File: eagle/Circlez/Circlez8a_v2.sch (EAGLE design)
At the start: 55 parts, among them IC1 MEGA8-AI, J1 AVR_SPI_PRG_6PTH

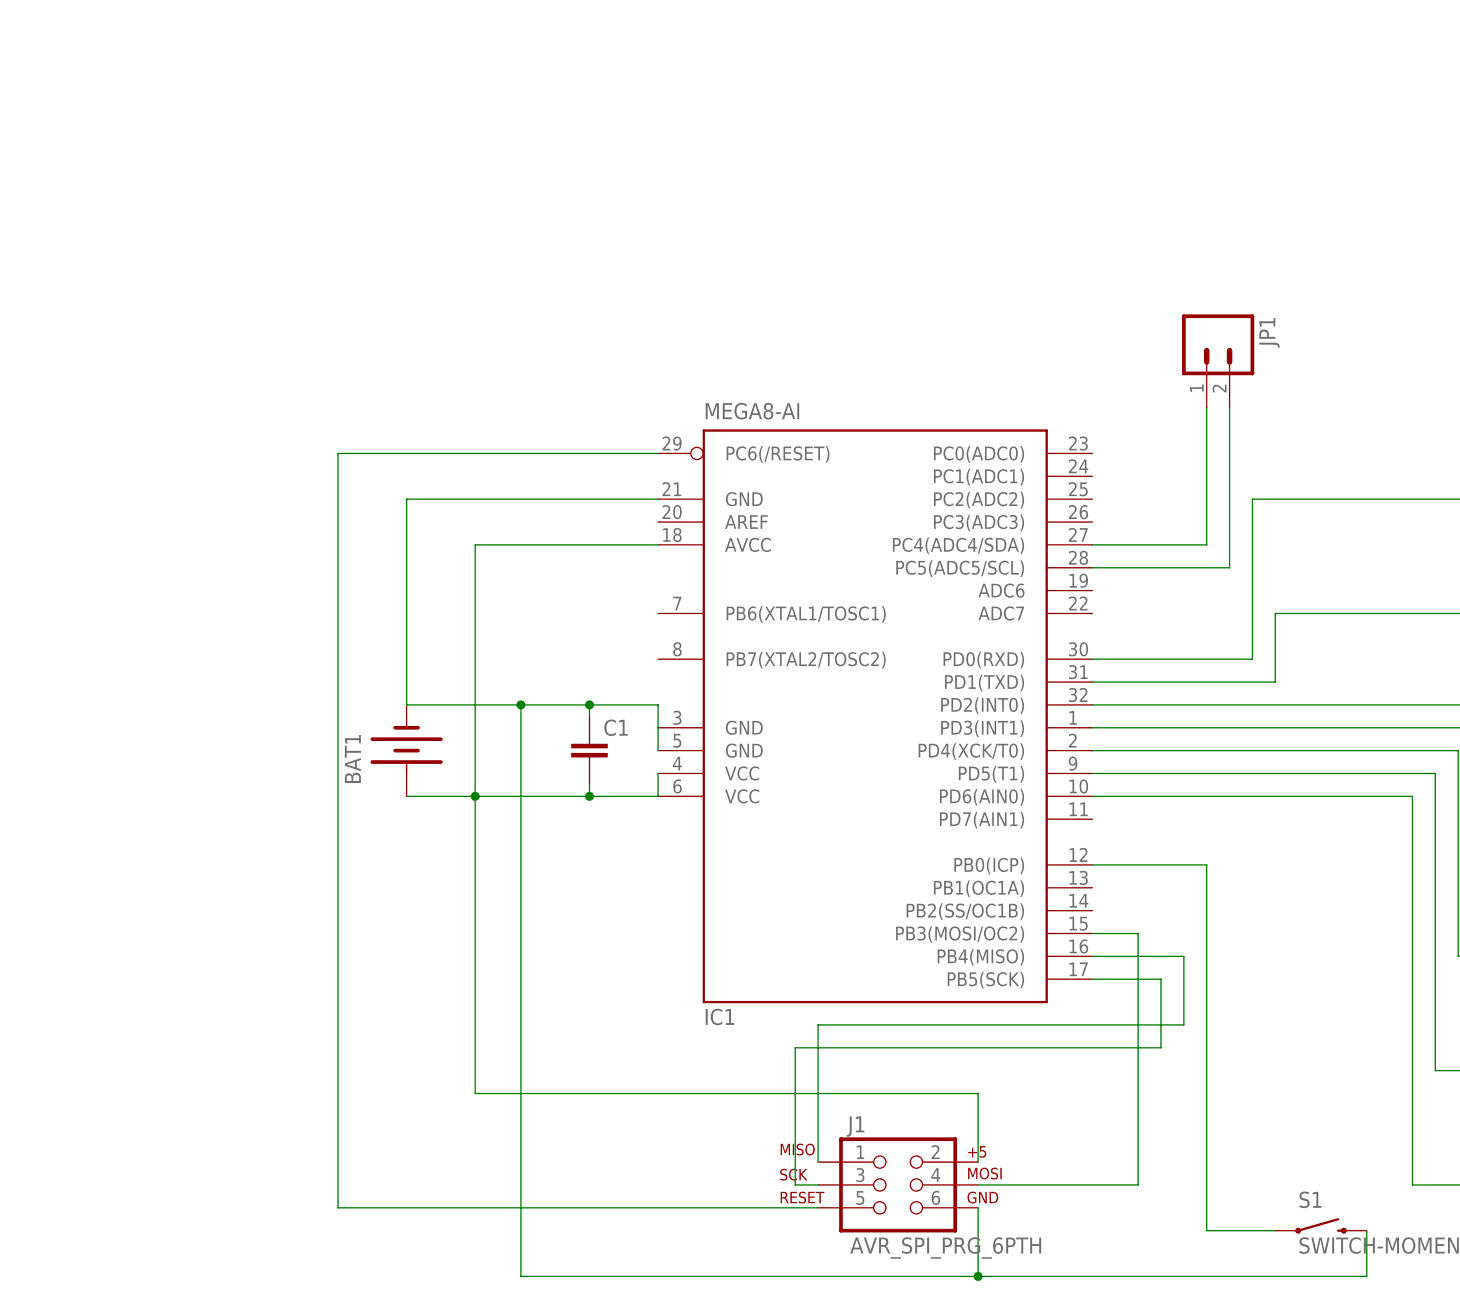
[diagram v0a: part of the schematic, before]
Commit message: Added DS1307 and pads for 5v.
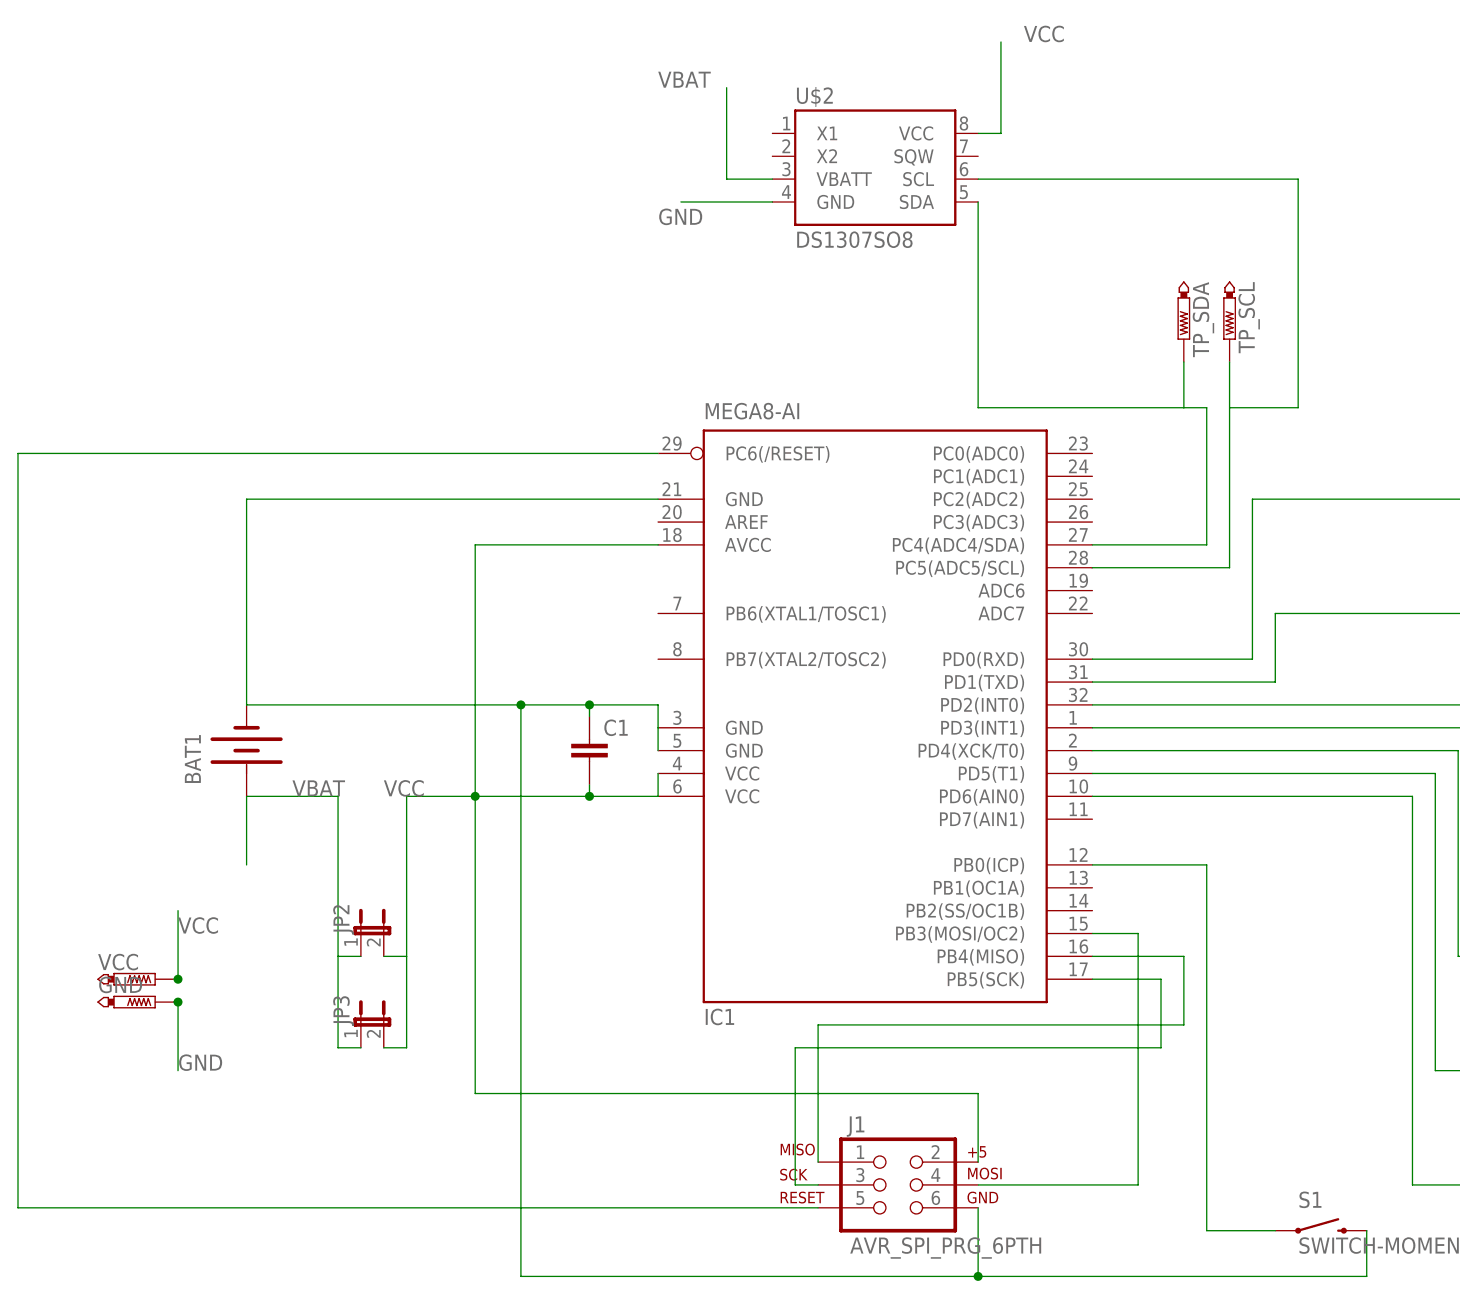
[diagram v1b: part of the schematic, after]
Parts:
- removed JP1: (no value), SparkFun-Connectors:M02PTH
- added GND, VCC: PTR1TP15SQ, testpad:PTR1TP15SQ
- added JP2: (no value), SparkFun-Passives:JUMPER-2SMD-NO
- added JP3: (no value), SparkFun-Passives:JUMPER-2PTH
- added TP_SCL, TP_SDA: PTR1TP09SQ, testpad:PTR1TP09SQ
- added U$2: DS1307SO8, SparkFun-FreqCtrl:DS1307SO8
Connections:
- removed net N$34: IC1.PC4(ADC4/SDA), JP1.1
- new net N$24: IC1.PC4(ADC4/SDA), TP_SDA.TP, U$2.SDA
- new net VBAT: BAT1.+, JP2.1, JP3.1, U$2.VBATT
- net GND: now also GND.TP, U$2.GND
- net N$12: now also TP_SCL.TP, U$2.SCL; no longer JP1.2
- net VCC: now also JP2.2, JP3.2, U$2.VCC, VCC.TP; no longer BAT1.+
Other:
- moved on the sheet: BAT1
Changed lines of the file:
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@@
 <layer number="106" name="bPlate" color="7" fill="1" visible="no" active="yes"/>
 <layer number="107" name="Crop" color="7" fill="1" visible="no" active="yes"/>
+<layer number="108" name="tplace-old" color="10" fill="1" visible="yes" active="yes"/>
+<layer number="109" name="ref-old" color="11" fill="1" visible="yes" active="yes"/>
 <layer number="116" name="Patch_BOT" color="9" fill="4" visible="no" active="yes"/>
 <layer number="121" name="_tsilk" color="7" fill="1" visible="no" active="yes"/>
@@
 <part name="C1" library="resistor" deviceset="C-EU" device="025-024X044"/>
 <part name="S1" library="SparkFun-Electromechanical" deviceset="SWITCH-MOMENTARY-2" device="PTH"/>
-<part name="JP1" library="SparkFun-Connectors" deviceset="M02" device="PTH"/>
 <part name="LED1" library="led" deviceset="LED" device="CHIPLED_0603"/>
 <part name="R1" library="resistor" deviceset="R-EU_" device="R1206"/>
@@
 <part name="HLED11" library="led" deviceset="LED" device="CHIP-LED0603"/>
 <part name="HLED12" library="led" deviceset="LED" device="CHIP-LED0603"/>
+<part name="U$2" library="SparkFun-FreqCtrl" deviceset="DS1307" device="SO8"/>
+<part name="JP2" library="SparkFun-Passives" deviceset="JUMPER-2" device="SMD-NO"/>
+<part name="JP3" library="SparkFun-Passives" deviceset="JUMPER-2" device="PTH"/>
+<part name="VCC" library="testpad" deviceset="PTR1" device="TP15SQ"/>
+<part name="GND" library="testpad" deviceset="PTR1" device="TP15SQ"/>
+<part name="TP_SDA" library="testpad" deviceset="PTR1" device="TP09SQ"/>
+<part name="TP_SCL" library="testpad" deviceset="PTR1" device="TP09SQ"/>
 </parts>
 <sheets>
@@
 <instances>
 <instance part="IC1" gate="G$1" x="106.68" y="45.72"/>
-<instance part="BAT1" gate="G$1" x="55.88" y="38.1" rot="R90"/>
+<instance part="BAT1" gate="G$1" x="38.1" y="38.1" rot="R90"/>
 <instance part="J1" gate="G$1" x="109.22" y="-10.16"/>
 <instance part="C1" gate="G$1" x="76.2" y="39.37"/>
 <instance part="S1" gate="G$1" x="157.48" y="-15.24"/>
-<instance part="JP1" gate="G$1" x="144.78" y="83.82" rot="R270"/>
 <instance part="LED1" gate="G$1" x="193.04" y="60.96"/>
 <instance part="R1" gate="G$1" x="182.88" y="66.04"/>
@@
 <instance part="HLED11" gate="G$1" x="523.24" y="53.34"/>
 <instance part="HLED12" gate="G$1" x="530.86" y="50.8" rot="R180"/>
+<instance part="U$2" gate="G$1" x="106.68" y="104.14"/>
+<instance part="JP2" gate="A" x="50.8" y="17.78"/>
+<instance part="JP3" gate="A" x="50.8" y="7.62"/>
+<instance part="VCC" gate="G$1" x="27.94" y="12.7" rot="R270"/>
+<instance part="GND" gate="G$1" x="27.94" y="10.16" rot="R270"/>
+<instance part="TP_SDA" gate="G$1" x="142.24" y="83.82" rot="R180"/>
+<instance part="TP_SCL" gate="G$1" x="147.32" y="83.82" rot="R180"/>
 </instances>
 <busses>
@@
 <net name="VCC" class="0">
 <segment>
-<pinref part="BAT1" gate="G$1" pin="+"/>
 <pinref part="IC1" gate="G$1" pin="VCC@2"/>
-<wire x1="55.88" y1="33.02" x2="63.5" y2="33.02" width="0.1524" layer="91"/>
 <pinref part="IC1" gate="G$1" pin="VCC@1"/>
 <wire x1="63.5" y1="33.02" x2="76.2" y2="33.02" width="0.1524" layer="91"/>
@@
 <wire x1="76.2" y1="33.02" x2="76.2" y2="34.29" width="0.1524" layer="91"/>
 <junction x="76.2" y="33.02"/>
+<pinref part="JP3" gate="A" pin="2"/>
+<wire x1="53.34" y1="5.08" x2="55.88" y2="5.08" width="0.1524" layer="91"/>
+<wire x1="55.88" y1="5.08" x2="55.88" y2="15.24" width="0.1524" layer="91"/>
+<pinref part="JP2" gate="A" pin="2"/>
+<wire x1="55.88" y1="15.24" x2="53.34" y2="15.24" width="0.1524" layer="91"/>
+<wire x1="55.88" y1="15.24" x2="55.88" y2="33.02" width="0.1524" layer="91"/>
+<wire x1="55.88" y1="33.02" x2="63.5" y2="33.02" width="0.1524" layer="91"/>
+<label x="53.34" y="33.02" size="1.778" layer="95"/>
+</segment>
+<segment>
+<wire x1="121.92" y1="106.68" x2="121.92" y2="116.84" width="0.1524" layer="91"/>
+<pinref part="U$2" gate="G$1" pin="VCC"/>
+<wire x1="119.38" y1="106.68" x2="121.92" y2="106.68" width="0.1524" layer="91"/>
+<label x="124.46" y="116.84" size="1.778" layer="95"/>
+</segment>
+<segment>
+<wire x1="30.48" y1="12.7" x2="30.48" y2="20.32" width="0.1524" layer="91"/>
+<label x="30.48" y="17.78" size="1.778" layer="95"/>
+<pinref part="VCC" gate="G$1" pin="TP"/>
+<junction x="30.48" y="12.7"/>
 </segment>
 </net>
@@
 <pinref part="BAT1" gate="G$1" pin="-"/>
 <pinref part="IC1" gate="G$1" pin="GND@1"/>
-<wire x1="55.88" y1="43.18" x2="68.58" y2="43.18" width="0.1524" layer="91"/>
+<wire x1="38.1" y1="43.18" x2="68.58" y2="43.18" width="0.1524" layer="91"/>
 <wire x1="68.58" y1="43.18" x2="76.2" y2="43.18" width="0.1524" layer="91"/>
 <wire x1="76.2" y1="43.18" x2="83.82" y2="43.18" width="0.1524" layer="91"/>
@@
 <pinref part="IC1" gate="G$1" pin="GND@2"/>
 <wire x1="83.82" y1="40.64" x2="83.82" y2="38.1" width="0.1524" layer="91"/>
-<wire x1="55.88" y1="43.18" x2="55.88" y2="66.04" width="0.1524" layer="91"/>
+<wire x1="38.1" y1="43.18" x2="38.1" y2="66.04" width="0.1524" layer="91"/>
 <pinref part="IC1" gate="G$1" pin="GND"/>
-<wire x1="55.88" y1="66.04" x2="83.82" y2="66.04" width="0.1524" layer="91"/>
+<wire x1="38.1" y1="66.04" x2="83.82" y2="66.04" width="0.1524" layer="91"/>
 <pinref part="J1" gate="G$1" pin="6"/>
 <wire x1="119.38" y1="-12.7" x2="119.38" y2="-20.32" width="0.1524" layer="91"/>
@@
 <junction x="119.38" y="-20.32"/>
 </segment>
+<segment>
+<pinref part="U$2" gate="G$1" pin="GND"/>
+<wire x1="96.52" y1="99.06" x2="86.36" y2="99.06" width="0.1524" layer="91"/>
+<label x="83.82" y="96.52" size="1.778" layer="95"/>
+</segment>
+<segment>
+<wire x1="30.48" y1="10.16" x2="30.48" y2="2.54" width="0.1524" layer="91"/>
+<label x="30.48" y="2.54" size="1.778" layer="95"/>
+<pinref part="GND" gate="G$1" pin="TP"/>
+<junction x="30.48" y="10.16"/>
+</segment>
 </net>
 <net name="N$3" class="0">
@@
 <segment>
 <pinref part="J1" gate="G$1" pin="5"/>
-<wire x1="101.6" y1="-12.7" x2="48.26" y2="-12.7" width="0.1524" layer="91"/>
-<wire x1="48.26" y1="-12.7" x2="48.26" y2="71.12" width="0.1524" layer="91"/>
+<wire x1="101.6" y1="-12.7" x2="12.7" y2="-12.7" width="0.1524" layer="91"/>
+<wire x1="12.7" y1="-12.7" x2="12.7" y2="71.12" width="0.1524" layer="91"/>
 <pinref part="IC1" gate="G$1" pin="PC6(/RESET)"/>
-<wire x1="48.26" y1="71.12" x2="83.82" y2="71.12" width="0.1524" layer="91"/>
+<wire x1="12.7" y1="71.12" x2="83.82" y2="71.12" width="0.1524" layer="91"/>
 </segment>
 </net>
@@
 </segment>
 </net>
-<net name="N$34" class="0">
-<segment>
-<pinref part="JP1" gate="G$1" pin="1"/>
+<net name="N$24" class="0">
+<segment>
 <wire x1="144.78" y1="60.96" x2="144.78" y2="76.2" width="0.1524" layer="91"/>
 <pinref part="IC1" gate="G$1" pin="PC4(ADC4/SDA)"/>
 <wire x1="132.08" y1="60.96" x2="144.78" y2="60.96" width="0.1524" layer="91"/>
+<pinref part="U$2" gate="G$1" pin="SDA"/>
+<wire x1="144.78" y1="76.2" x2="142.24" y2="76.2" width="0.1524" layer="91"/>
+<wire x1="142.24" y1="76.2" x2="119.38" y2="76.2" width="0.1524" layer="91"/>
+<wire x1="119.38" y1="76.2" x2="119.38" y2="99.06" width="0.1524" layer="91"/>
+<pinref part="TP_SDA" gate="G$1" pin="TP"/>
+<wire x1="142.24" y1="76.2" x2="142.24" y2="81.28" width="0.1524" layer="91"/>
 </segment>
 </net>
 <net name="N$12" class="0">
 <segment>
-<pinref part="JP1" gate="G$1" pin="2"/>
 <wire x1="147.32" y1="58.42" x2="147.32" y2="76.2" width="0.1524" layer="91"/>
 <pinref part="IC1" gate="G$1" pin="PC5(ADC5/SCL)"/>
 <wire x1="147.32" y1="58.42" x2="132.08" y2="58.42" width="0.1524" layer="91"/>
+<wire x1="147.32" y1="76.2" x2="154.94" y2="76.2" width="0.1524" layer="91"/>
+<wire x1="154.94" y1="76.2" x2="154.94" y2="101.6" width="0.1524" layer="91"/>
+<pinref part="U$2" gate="G$1" pin="SCL"/>
+<wire x1="154.94" y1="101.6" x2="119.38" y2="101.6" width="0.1524" layer="91"/>
+<pinref part="TP_SCL" gate="G$1" pin="TP"/>
+<wire x1="147.32" y1="76.2" x2="147.32" y2="81.28" width="0.1524" layer="91"/>
 </segment>
 </net>
@@
 </segment>
 </net>
+<net name="VBAT" class="0">
+<segment>
+<pinref part="U$2" gate="G$1" pin="VBATT"/>
+<wire x1="96.52" y1="101.6" x2="91.44" y2="101.6" width="0.1524" layer="91"/>
+<wire x1="91.44" y1="101.6" x2="91.44" y2="111.76" width="0.1524" layer="91"/>
+<label x="83.82" y="111.76" size="1.778" layer="95"/>
+</segment>
+<segment>
+<pinref part="JP2" gate="A" pin="1"/>
+<wire x1="50.8" y1="15.24" x2="48.26" y2="15.24" width="0.1524" layer="91"/>
+<wire x1="48.26" y1="15.24" x2="48.26" y2="5.08" width="0.1524" layer="91"/>
+<pinref part="JP3" gate="A" pin="1"/>
+<wire x1="48.26" y1="5.08" x2="50.8" y2="5.08" width="0.1524" layer="91"/>
+<wire x1="48.26" y1="15.24" x2="48.26" y2="33.02" width="0.1524" layer="91"/>
+<pinref part="BAT1" gate="G$1" pin="+"/>
+<wire x1="38.1" y1="33.02" x2="38.1" y2="25.4" width="0.1524" layer="91"/>
+<wire x1="48.26" y1="33.02" x2="38.1" y2="33.02" width="0.1524" layer="91"/>
+<label x="43.18" y="33.02" size="1.778" layer="95"/>
+</segment>
+</net>

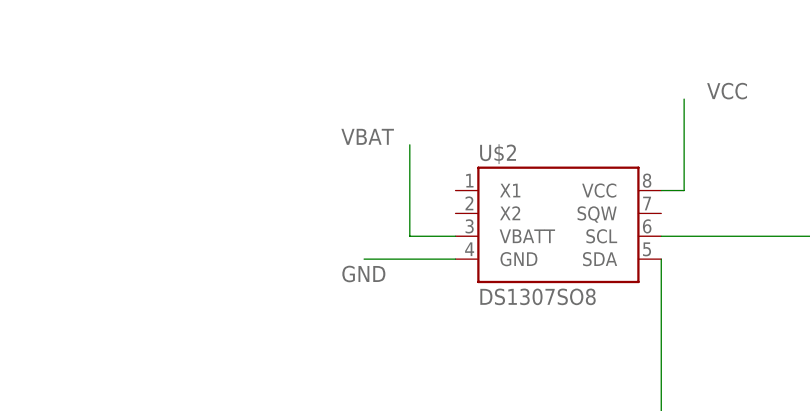
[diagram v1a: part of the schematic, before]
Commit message: New version with wires farther from the border, ready for prod.
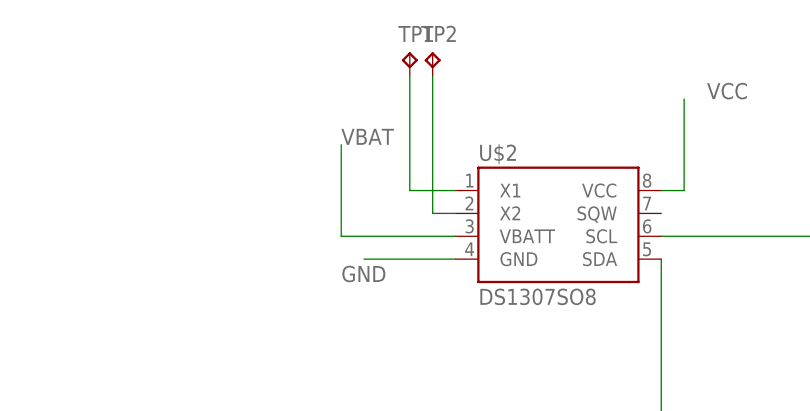
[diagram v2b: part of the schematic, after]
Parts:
- added TP1, TP2: TPTP13SQ, testpad:TPTP13SQ
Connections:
- new net N$22: TP1.TP, U$2.X1
- new net N$23: TP2.TP, U$2.X2
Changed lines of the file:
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@@
 <part name="TP_SDA" library="testpad" deviceset="PTR1" device="TP09SQ"/>
 <part name="TP_SCL" library="testpad" deviceset="PTR1" device="TP09SQ"/>
+<part name="TP1" library="testpad" deviceset="TP" device="TP13SQ" value="TPTP13SQ"/>
+<part name="TP2" library="testpad" deviceset="TP" device="TP13SQ" value="TPTP13SQ"/>
 </parts>
 <sheets>
@@
 <instance part="TP_SDA" gate="G$1" x="142.24" y="83.82" rot="R180"/>
 <instance part="TP_SCL" gate="G$1" x="147.32" y="83.82" rot="R180"/>
+<instance part="TP1" gate="G$1" x="91.44" y="121.92"/>
+<instance part="TP2" gate="G$1" x="93.98" y="121.92"/>
 </instances>
 <busses>
@@
 <segment>
 <pinref part="U$2" gate="G$1" pin="VBATT"/>
-<wire x1="96.52" y1="101.6" x2="91.44" y2="101.6" width="0.1524" layer="91"/>
-<wire x1="91.44" y1="101.6" x2="91.44" y2="111.76" width="0.1524" layer="91"/>
+<wire x1="96.52" y1="101.6" x2="83.82" y2="101.6" width="0.1524" layer="91"/>
+<wire x1="83.82" y1="101.6" x2="83.82" y2="111.76" width="0.1524" layer="91"/>
 <label x="83.82" y="111.76" size="1.778" layer="95"/>
 </segment>
@@
 </segment>
 </net>
+<net name="N$22" class="0">
+<segment>
+<pinref part="TP1" gate="G$1" pin="TP"/>
+<wire x1="91.44" y1="119.38" x2="91.44" y2="106.68" width="0.1524" layer="91"/>
+<pinref part="U$2" gate="G$1" pin="X1"/>
+<wire x1="91.44" y1="106.68" x2="96.52" y2="106.68" width="0.1524" layer="91"/>
+</segment>
+</net>
+<net name="N$23" class="0">
+<segment>
+<pinref part="TP2" gate="G$1" pin="TP"/>
+<wire x1="93.98" y1="119.38" x2="93.98" y2="104.14" width="0.1524" layer="91"/>
+<pinref part="U$2" gate="G$1" pin="X2"/>
+<wire x1="93.98" y1="104.14" x2="96.52" y2="104.14" width="0.1524" layer="91"/>
+</segment>
+</net>
